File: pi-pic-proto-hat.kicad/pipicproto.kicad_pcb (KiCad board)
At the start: 2 copper layers, 65 x 56 mm, 20 parts, among them J1 RUN/~PGM~, J10 Conn_01x13_Male, J22 Conn_01x13_Male, J6 Barrel_Jack_Switch, J7 Conn_01x24_Male, J8 Conn_01x06_Male, J9 Conn_01x02_Male, P1 Conn_02x20_Odd_Even, Q1 IRF4905, U1 PIC12F675-IP

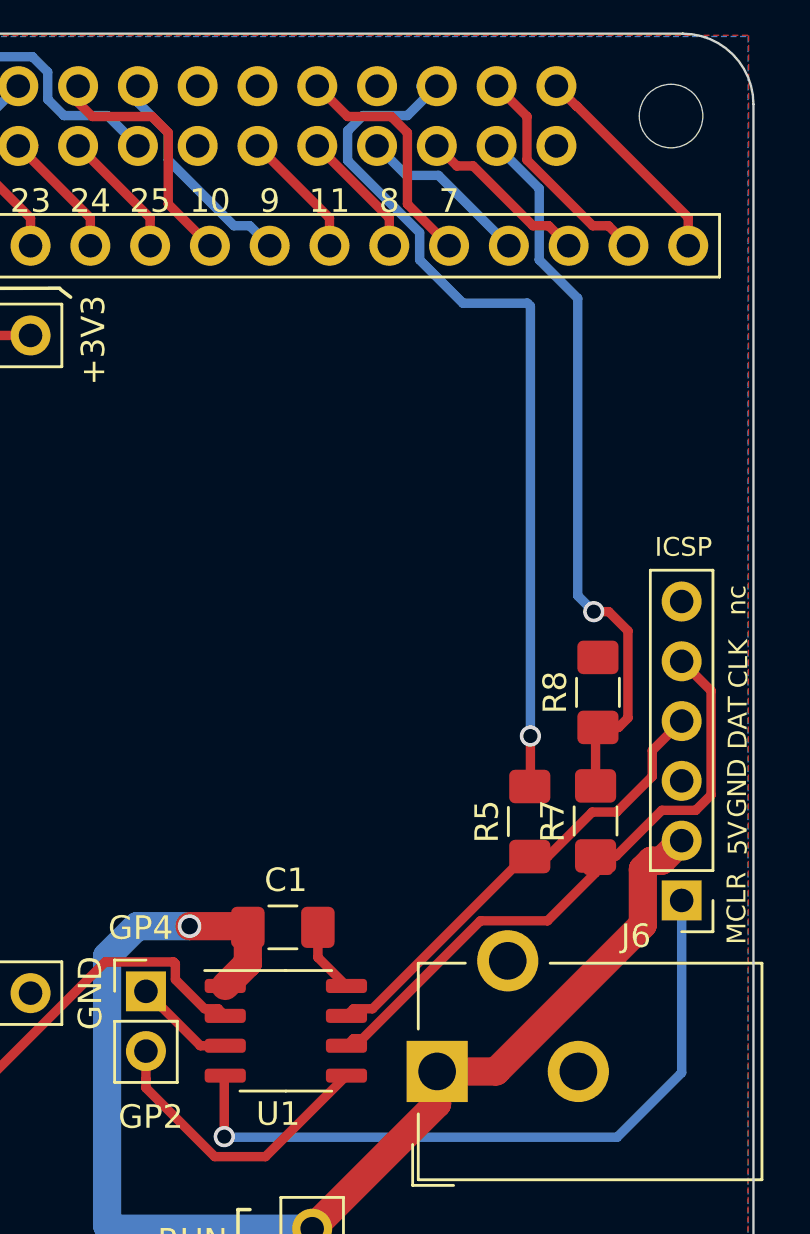
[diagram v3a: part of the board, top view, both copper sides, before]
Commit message: moved R7/R8 to top right
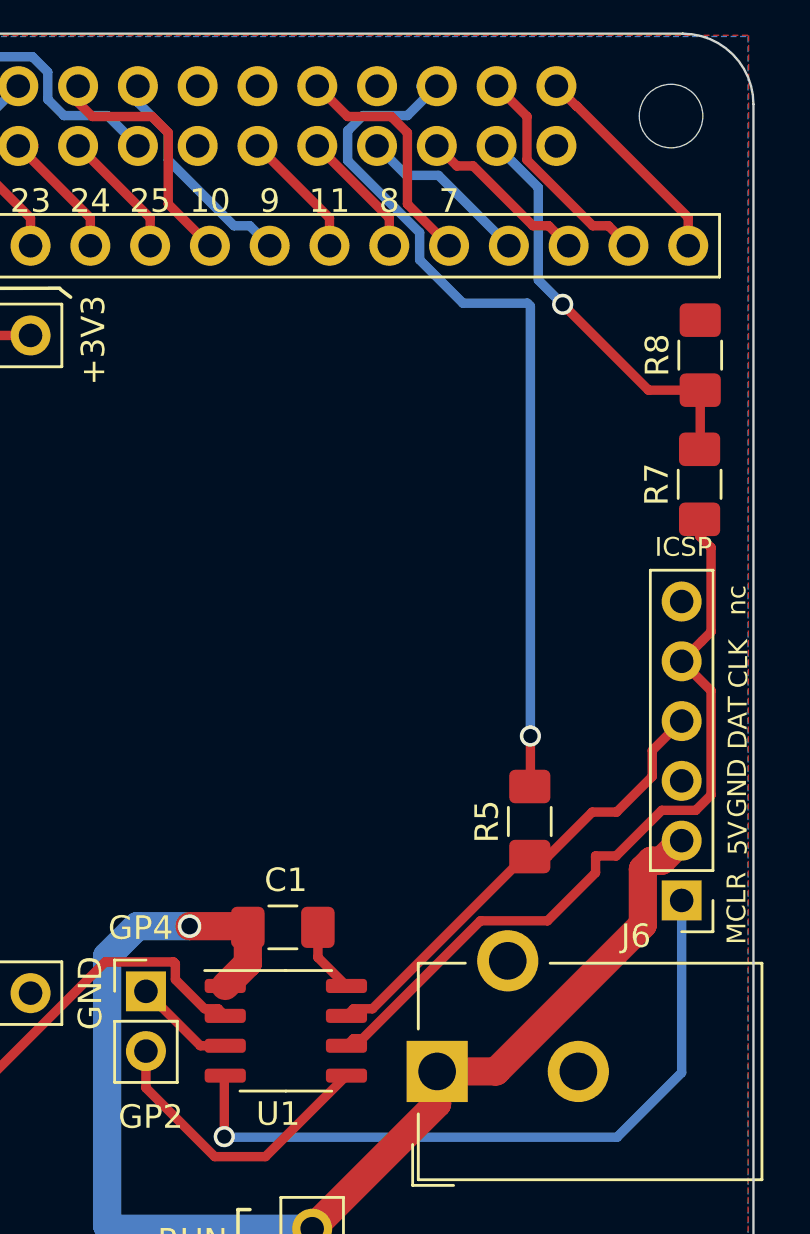
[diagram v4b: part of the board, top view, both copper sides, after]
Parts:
- moved R8 15.0 mm to (262.7, 107.7)
- moved R7 15.0 mm to (262.7, 113.1)
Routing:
- net /GPIO26: track 31.4 -> 17.8 mm
- net /CLK: track 27.4 -> 33.3 mm
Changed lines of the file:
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@@
     (thickness 1.6)
     (drawings 67)
-    (tracks 233)
+    (tracks 230)
     (zones 0)
     (modules 20)
@@
   )
   (module Resistor_SMD:R_1206_3216Metric_Pad1.42x1.75mm_HandSolder (layer F.Cu)
-    (at 258.3946 121.9838 90)
+    (at 262.738 107.6582 90)
     (descr "Resistor SMD 1206 (3216 Metric), square (rectangular) end terminal, IPC_7351 nominal with elongated pad for handsoldering. (Body size source: http://www.tortai-tech.com/upload/download/2011102023233369053.pdf), generated with kicad-footprint-generator")
     (tags "resistor handsolder")
@@
   )
   (module Resistor_SMD:R_1206_3216Metric_Pad1.42x1.75mm_HandSolder (layer F.Cu)
-    (at 258.293 127.4448 90)
+    (at 262.7126 113.1446 90)
     (descr "Resistor SMD 1206 (3216 Metric), square (rectangular) end terminal, IPC_7351 nominal with elongated pad for handsoldering. (Body size source: http://www.tortai-tech.com/upload/download/2011102023233369053.pdf), generated with kicad-footprint-generator")
     (tags "resistor handsolder")
@@
   (segment (start 249.53 101.83) (end 249.53 103.01) (width 0.4) (layer F.Cu) (net 7) (status 20))
   (segment (start 246.47 98.77) (end 249.53 101.83) (width 0.4) (layer F.Cu) (net 7) (status 10))
-  (segment (start 258.293 125.502) (end 258.293 125.9573) (width 0.4) (layer F.Cu) (net 8) (status 30))
-  (segment (start 255.899999 103.610001) (end 257.535198 105.2452) (width 0.4) (layer B.Cu) (net 8))
-  (segment (start 254.09 98.77) (end 255.899999 100.579999) (width 0.4) (layer B.Cu) (net 8) (status 10))
-  (segment (start 255.899999 100.579999) (end 255.899999 103.610001) (width 0.4) (layer B.Cu) (net 8))
-  (via (at 258.2168 118.5548) (size 0.9) (drill 0.6) (layers F.Cu B.Cu) (net 8))
-  (segment (start 257.535198 105.2452) (end 257.535198 117.873198) (width 0.4) (layer B.Cu) (net 8))
-  (segment (start 257.535198 117.873198) (end 258.2168 118.5548) (width 0.4) (layer B.Cu) (net 8))
-  (segment (start 259.2696 123.4713) (end 258.3946 123.4713) (width 0.4) (layer F.Cu) (net 8) (status 20))
-  (segment (start 259.66961 123.07129) (end 259.2696 123.4713) (width 0.4) (layer F.Cu) (net 8))
-  (segment (start 259.66961 119.371214) (end 259.66961 123.07129) (width 0.4) (layer F.Cu) (net 8))
-  (segment (start 258.853196 118.5548) (end 259.66961 119.371214) (width 0.4) (layer F.Cu) (net 8))
-  (segment (start 258.2168 118.5548) (end 258.853196 118.5548) (width 0.4) (layer F.Cu) (net 8))
-  (segment (start 258.293 123.5729) (end 258.3946 123.4713) (width 0.4) (layer F.Cu) (net 8) (status 30))
-  (segment (start 258.293 125.9573) (end 258.293 123.5729) (width 0.4) (layer F.Cu) (net 8) (status 30))
+  (via (at 256.896 105.4992) (size 0.9) (drill 0.6) (layers F.Cu B.Cu) (net 8))
+  (segment (start 254.09 98.77) (end 255.860001 100.540001) (width 0.4) (layer B.Cu) (net 8))
+  (segment (start 255.860001 104.463201) (end 256.896 105.4992) (width 0.4) (layer B.Cu) (net 8))
+  (segment (start 255.860001 100.540001) (end 255.860001 104.463201) (width 0.4) (layer B.Cu) (net 8))
+  (segment (start 260.5425 109.1457) (end 262.738 109.1457) (width 0.4) (layer F.Cu) (net 8))
+  (segment (start 256.896 105.4992) (end 260.5425 109.1457) (width 0.4) (layer F.Cu) (net 8))
+  (segment (start 262.738 111.6317) (end 262.7126 111.6571) (width 0.4) (layer F.Cu) (net 8))
+  (segment (start 262.738 109.1457) (end 262.738 111.6317) (width 0.4) (layer F.Cu) (net 8))
   (segment (start 206.799999 100.020001) (end 203.81 103.01) (width 0.4) (layer F.Cu) (net 9) (status 20))
   (segment (start 209.659999 100.020001) (end 206.799999 100.020001) (width 0.4) (layer F.Cu) (net 9))
@@
   (segment (start 237.542199 144.632001) (end 237.542199 133.193799) (width 1.2) (layer B.Cu) (net 30))
   (segment (start 237.677798 144.7676) (end 237.542199 144.632001) (width 1.2) (layer B.Cu) (net 30))
-  (segment (start 257.9628 129.5419) (end 258.8378 129.5419) (width 0.4) (layer F.Cu) (net 33) (status 30))
   (segment (start 263.200601 121.913001) (end 261.9506 120.663) (width 0.4) (layer F.Cu) (net 33) (status 20))
   (segment (start 263.200601 126.343001) (end 263.200601 121.913001) (width 0.4) (layer F.Cu) (net 33))
@@
   (segment (start 261.107299 126.993001) (end 262.550601 126.993001) (width 0.4) (layer F.Cu) (net 33))
   (segment (start 259.168 128.9323) (end 261.107299 126.993001) (width 0.4) (layer F.Cu) (net 33))
-  (segment (start 258.293 128.9323) (end 259.168 128.9323) (width 0.4) (layer F.Cu) (net 33) (status 10))
+  (segment (start 258.293 128.9323) (end 259.168 128.9323) (width 0.4) (layer F.Cu) (net 33))
   (segment (start 248.393634 136.6952) (end 248.0108 136.6952) (width 0.4) (layer F.Cu) (net 33) (status 30))
   (segment (start 253.401435 131.687399) (end 248.393634 136.6952) (width 0.4) (layer F.Cu) (net 33) (status 20))
@@
   (segment (start 248.0108 136.6952) (end 247.7108 136.9952) (width 0.4) (layer F.Cu) (net 33) (status 30))
   (segment (start 256.250401 131.687399) (end 253.401435 131.687399) (width 0.4) (layer F.Cu) (net 33))
-  (segment (start 258.293 128.9323) (end 258.293 129.6448) (width 0.4) (layer F.Cu) (net 33) (status 10))
+  (segment (start 258.293 128.9323) (end 258.293 129.6448) (width 0.4) (layer F.Cu) (net 33))
+  (segment (start 262.800599 119.813001) (end 261.9506 120.663) (width 0.4) (layer F.Cu) (net 33))
+  (segment (start 263.200601 119.412999) (end 262.800599 119.813001) (width 0.4) (layer F.Cu) (net 33))
+  (segment (start 263.200601 115.832601) (end 263.200601 119.412999) (width 0.4) (layer F.Cu) (net 33))
+  (segment (start 262.7126 115.3446) (end 263.200601 115.832601) (width 0.4) (layer F.Cu) (net 33))
+  (segment (start 262.7126 114.6321) (end 262.7126 115.3446) (width 0.4) (layer F.Cu) (net 33))
   (segment (start 261.8379 123.0903) (end 261.9506 123.203) (width 0.4) (layer F.Cu) (net 34) (status 30))
   (segment (start 260.700599 124.453001) (end 261.9506 123.203) (width 0.4) (layer F.Cu) (net 34) (status 20))
@@
   (segment (start 240.442201 134.181201) (end 240.442201 133.513799) (width 0.4) (layer F.Cu) (net 38))
   (segment (start 241.6862 135.4252) (end 240.442201 134.181201) (width 0.4) (layer F.Cu) (net 38))
-  (segment (start 223.4299 141.6066) (end 223.4299 142.4816) (width 0.4) (layer F.Cu) (net 38))
-  (segment (start 242.2608 135.4252) (end 241.6862 135.4252) (width 0.4) (layer F.Cu) (net 38))
-  (segment (start 223.88071 141.15579) (end 223.4299 141.6066) (width 0.4) (layer F.Cu) (net 38))
-  (segment (start 242.5608 135.7252) (end 242.2608 135.4252) (width 0.4) (layer F.Cu) (net 38))
+  (segment (start 223.4299 141.6066) (end 223.4299 142.4816) (width 0.4) (layer F.Cu) (net 38) (status 30))
+  (segment (start 242.2608 135.4252) (end 241.6862 135.4252) (width 0.4) (layer F.Cu) (net 38) (status 10))
+  (segment (start 223.88071 141.15579) (end 223.4299 141.6066) (width 0.4) (layer F.Cu) (net 38) (status 20))
+  (segment (start 242.5608 135.7252) (end 242.2608 135.4252) (width 0.4) (layer F.Cu) (net 38) (status 30))
   (segment (start 240.139999 101.239999) (end 241.91 103.01) (width 0.4) (layer F.Cu) (net 39) (status 20))
   (segment (start 240.139999 98.209997) (end 240.139999 101.239999) (width 0.4) (layer F.Cu) (net 39))
@@
   (segment (start 238.85 96.919998) (end 240.139999 98.209997) (width 0.4) (layer B.Cu) (net 40) (status 10))
   (segment (start 238.85 96.23) (end 238.85 96.919998) (width 0.4) (layer B.Cu) (net 40) (status 30))
-  (segment (start 239.1922 138.425881) (end 239.1922 137.2238) (width 0.4) (layer F.Cu) (net 41))
-  (segment (start 239.1922 138.786602) (end 239.1922 138.425881) (width 0.4) (layer F.Cu) (net 41))
+  (segment (start 239.1922 138.786602) (end 239.1922 137.2238) (width 0.4) (layer F.Cu) (net 41) (status 20))
   (segment (start 242.111599 141.706001) (end 239.1922 138.786602) (width 0.4) (layer F.Cu) (net 41))
   (segment (start 244.269999 141.706001) (end 242.111599 141.706001) (width 0.4) (layer F.Cu) (net 41))
-  (segment (start 247.7108 138.2652) (end 244.269999 141.706001) (width 0.4) (layer F.Cu) (net 41))
-  (segment (start 241.5036 136.9952) (end 242.5608 136.9952) (width 0.4) (layer F.Cu) (net 42))
-  (segment (start 239.1922 134.6838) (end 241.5036 136.9952) (width 0.4) (layer F.Cu) (net 42))
+  (segment (start 247.7108 138.2652) (end 244.269999 141.706001) (width 0.4) (layer F.Cu) (net 41) (status 10))
+  (segment (start 241.5036 136.9952) (end 242.5608 136.9952) (width 0.4) (layer F.Cu) (net 42) (status 20))
+  (segment (start 239.1922 134.6838) (end 241.5036 136.9952) (width 0.4) (layer F.Cu) (net 42) (status 10))
   (segment (start 231.6039 147.333) (end 230.2514 147.333) (width 0.4) (layer F.Cu) (net 43) (status 20))
   (segment (start 231.8913 147.0456) (end 231.6039 147.333) (width 0.4) (layer F.Cu) (net 43))

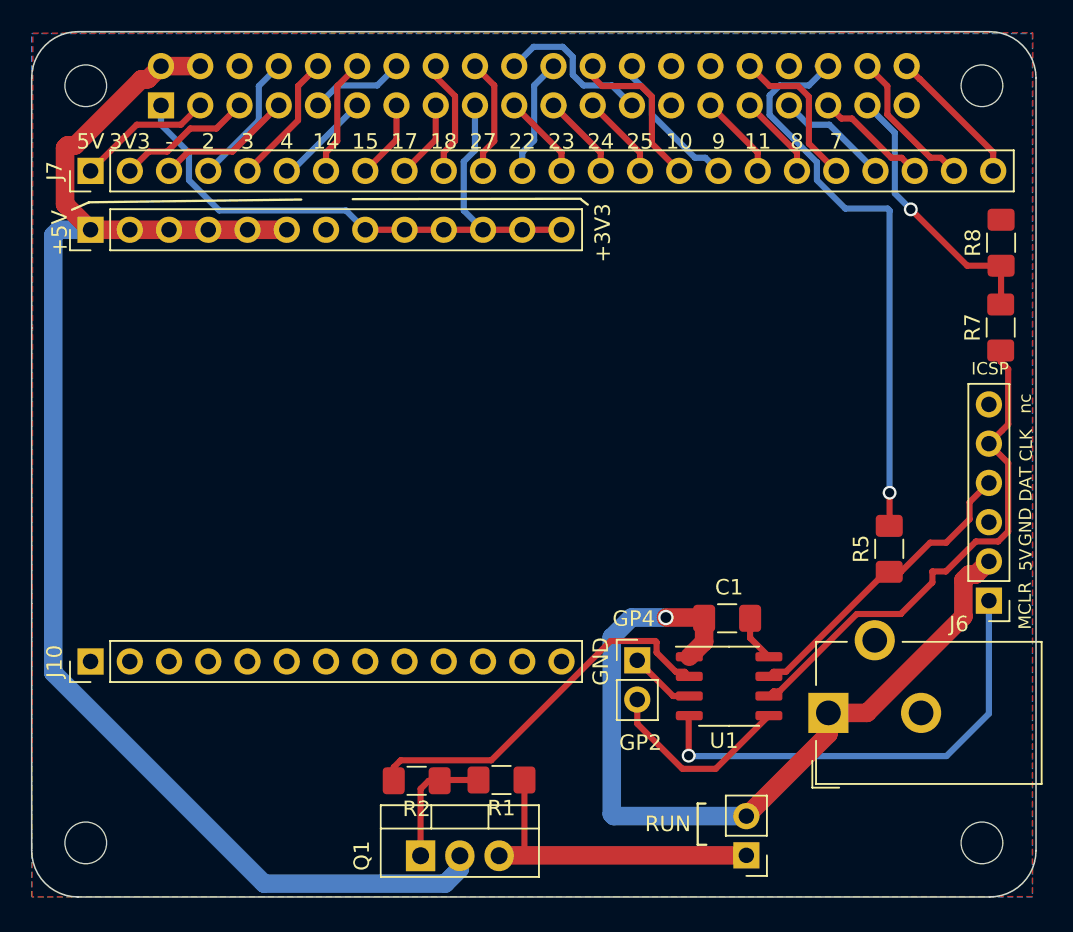
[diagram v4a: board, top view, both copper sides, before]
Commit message: moved R5/PIC next to ICSP
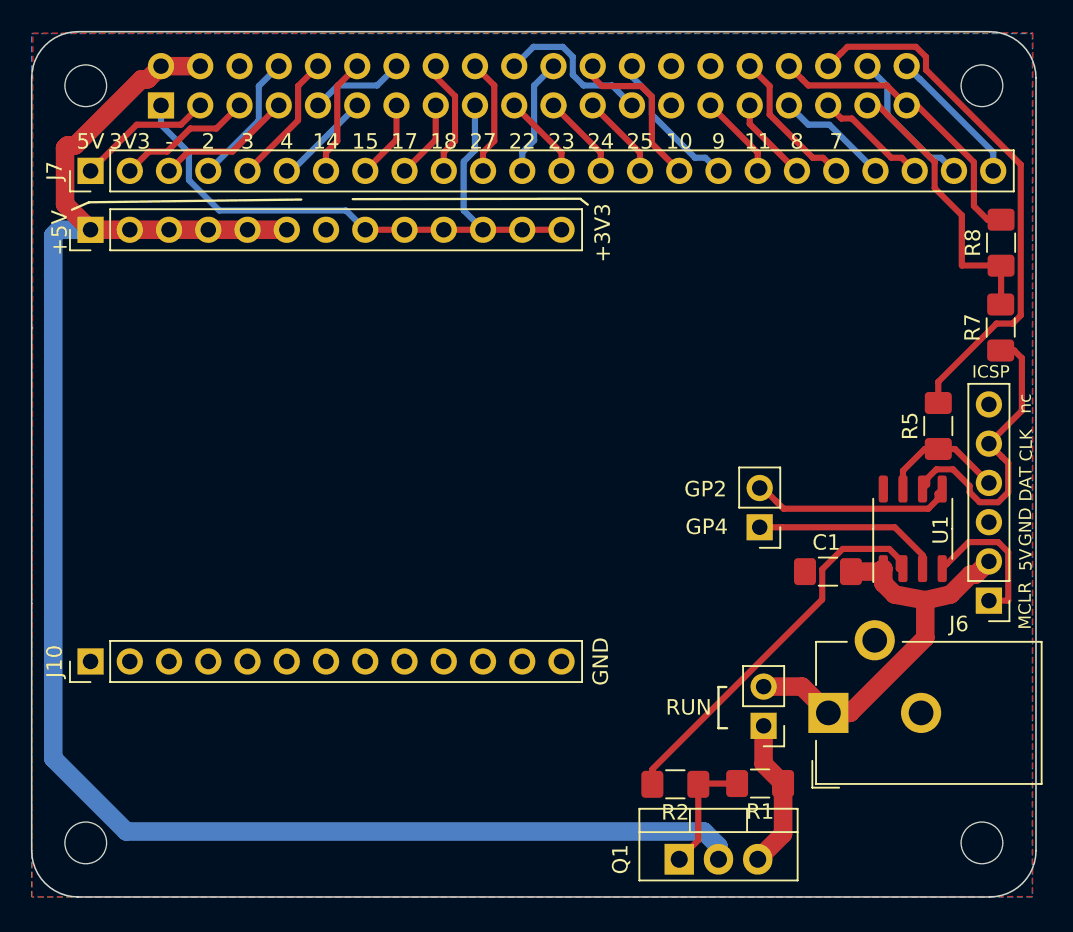
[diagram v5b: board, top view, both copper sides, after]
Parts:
- moved R1 16.7 mm to (247.1, 142.7)
- moved R2 16.7 mm to (241.7, 142.7)
- moved Q1 16.7 mm to (241.9, 147.6)
- moved U1 15.7 mm to (257.0, 126.2), turned to 90 degrees
- moved J9 11.7 mm to (247.1, 126.1), turned to 180 degrees
- moved R5 8.56 mm to (258.7, 119.5)
- moved J1 8.46 mm to (247.4, 138.9)
- moved C1 7.19 mm to (251.5, 128.9), turned to 0 degrees
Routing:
- net +5VP: track 54.3 -> 26.8 mm, vias 1 -> 0
- net /MCLR: track 30.5 -> 9.64 mm, vias 1 -> 0
- net +5V: track 93.7 -> 112.3 mm
- net GND: track 19.6 -> 36.0 mm
- net /CLK: track 33.3 -> 19.3 mm
- net +5P: track 22.4 -> 9.84 mm
- net /DAT: track 20.2 -> 8.27 mm
- net Net-(J9-Pad1): track 4.33 -> 12.0 mm
- net /GPIO16: track 38.0 -> 34.9 mm, vias 1 -> 0
- net Net-(Q1-Pad1): track 8.77 -> 7.89 mm
- net /GPIO12(PWM0): track 10.2 -> 9.49 mm
- net /GPIO26: track 17.8 -> 18.4 mm, vias 1 -> 0

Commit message: V2.11: added LEDs
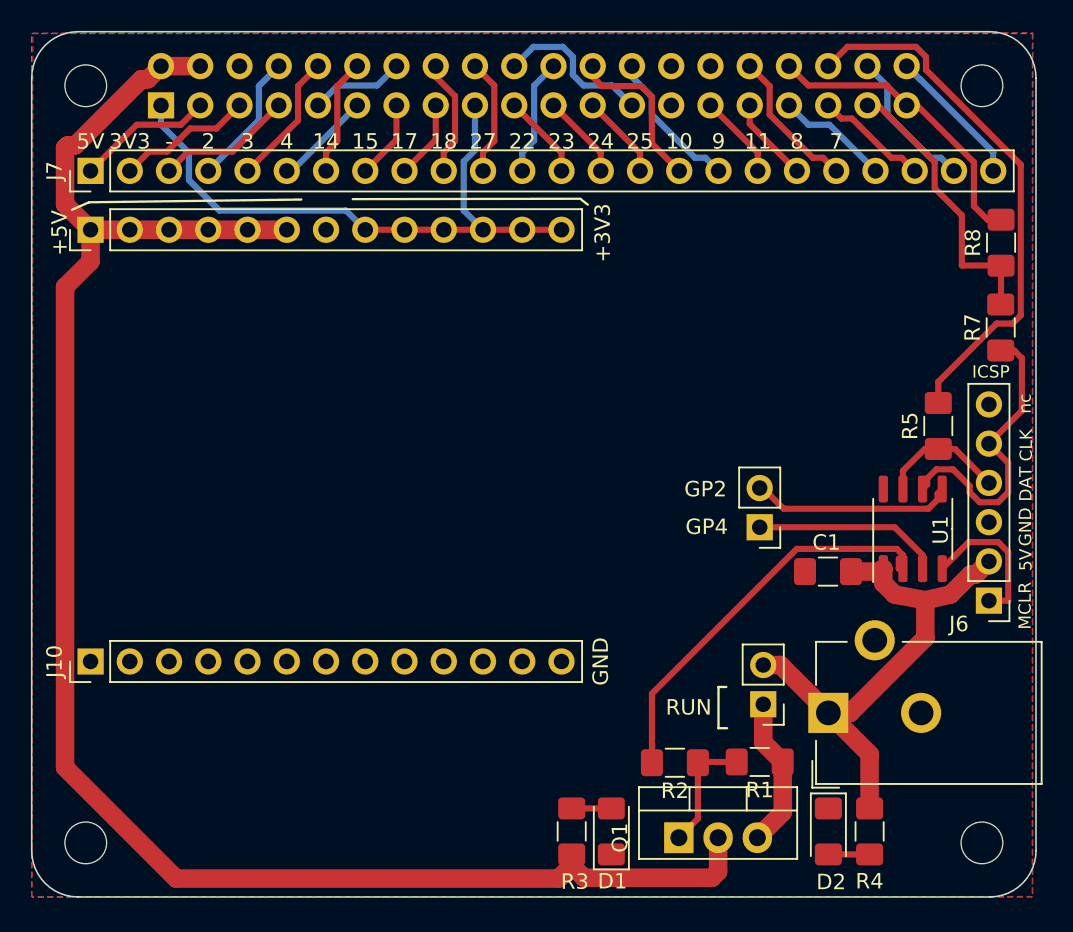
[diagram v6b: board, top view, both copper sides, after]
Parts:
- added D1: LED, LED_SMD:LED_1206_3216Metric_Pad1.42x1.75mm_HandSolder, F.Cu at (237.5, 145.8)
- added D2: LED, LED_SMD:LED_1206_3216Metric_Pad1.42x1.75mm_HandSolder, F.Cu at (251.6, 145.8)
- added R3: 1k, Resistor_SMD:R_1206_3216Metric_Pad1.42x1.75mm_HandSolder, F.Cu at (235.0, 145.8)
- added R4: 1k, Resistor_SMD:R_1206_3216Metric_Pad1.42x1.75mm_HandSolder, F.Cu at (254.2, 145.8)
- moved J1 1.40 mm to (247.3, 137.5)
- moved R1 1.40 mm to (247.1, 141.3)
- moved R2 1.40 mm to (241.6, 141.3)
- moved Q1 1.40 mm to (241.9, 146.2)
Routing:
- net +5VP: track 26.8 -> 34.7 mm
- net Net-(D2-Pad2): track 0.00 -> 2.67 mm
- net Net-(D1-Pad2): track 0.00 -> 2.57 mm
- net +5V: track 112.3 -> 114.1 mm
- net Net-(R2-Pad2): track 25.1 -> 26.7 mm
